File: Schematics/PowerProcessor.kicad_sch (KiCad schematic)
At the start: 0 parts

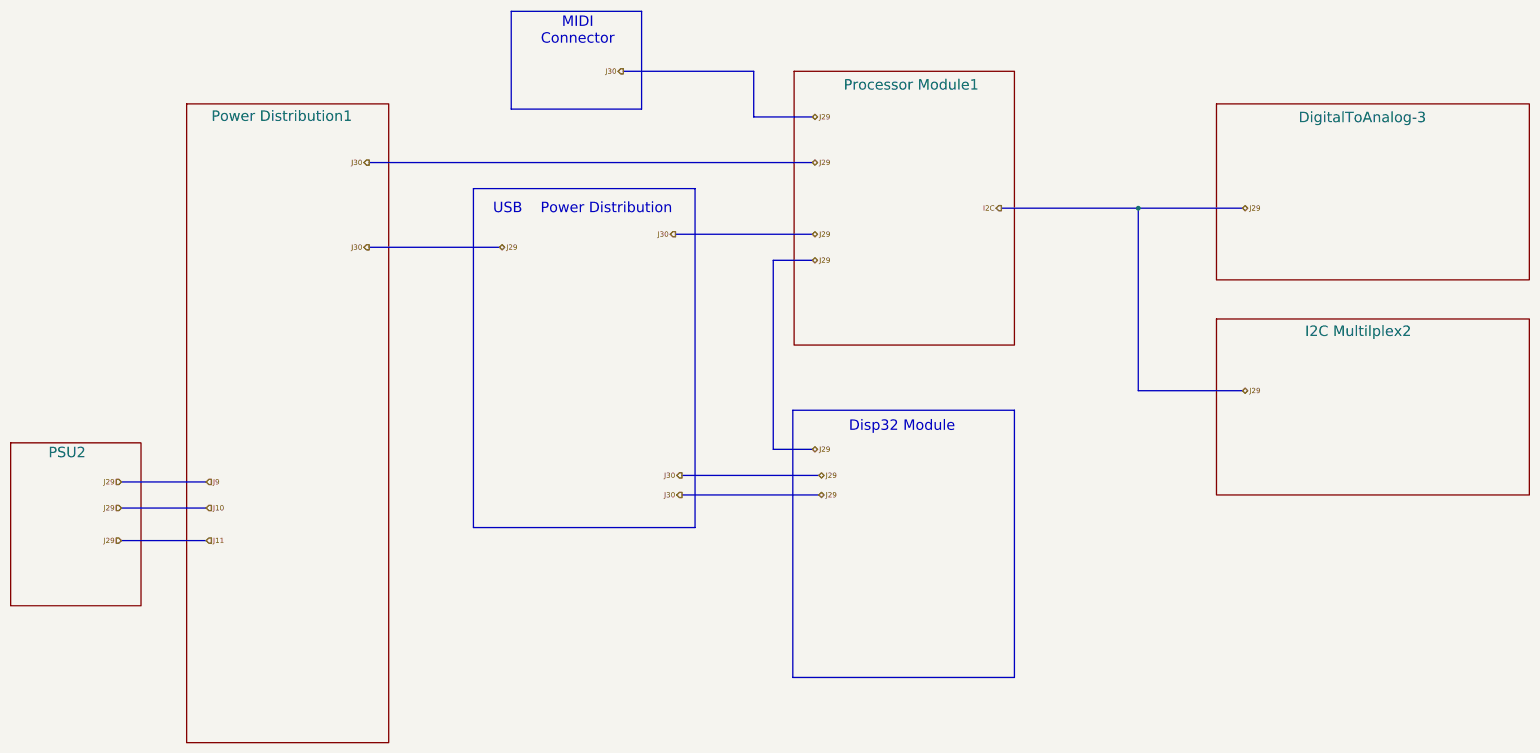
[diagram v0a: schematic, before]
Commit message: Updated schematics.  Added modulation control to VCF.
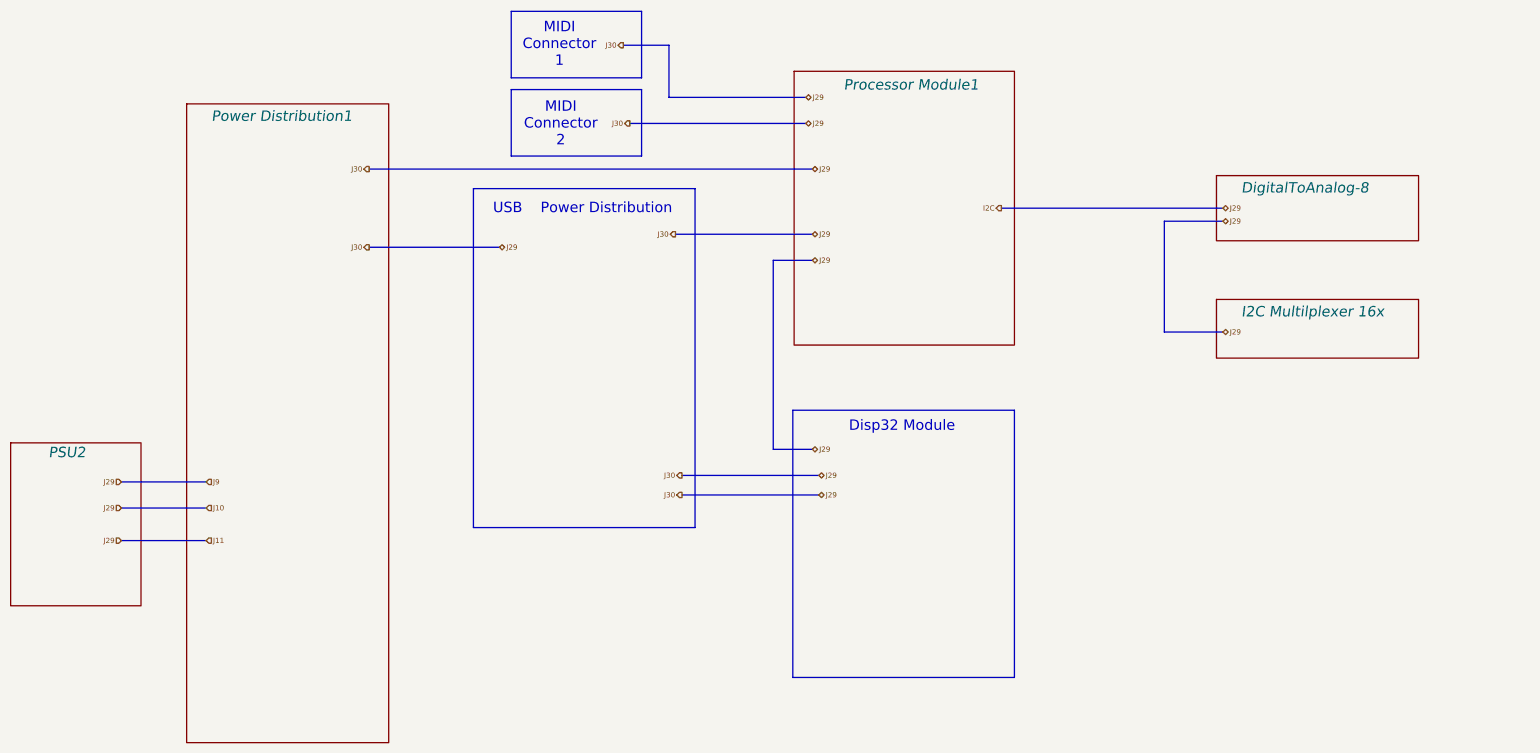
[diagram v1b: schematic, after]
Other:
- sheet DigitalToAnalog-3 renamed DigitalToAnalog-8
- sheet I2C Multilplex2 renamed I2C Multilplexer 16x
- note added: "MIDI Connector 1"
- note added: "MIDI Connector 2"
- note removed: "MIDI Connector"
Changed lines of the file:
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@@
 	(rectangle
 		(start 120.396 16.256)
-		(end 145.796 35.306)
+		(end 145.796 29.21)
 		(stroke
 			(width 0)
@@
 		)
 	)
-	(text "MIDI\nConnector"
-		(exclude_from_sim no)
-		(at 133.35 22.86 0)
+	(rectangle
+		(start 120.396 31.496)
+		(end 145.796 44.45)
+		(stroke
+			(width 0)
+			(type default)
+		)
+		(fill
+			(type none)
+		)
+	)
+	(text "MIDI\nConnector\n1"
+		(exclude_from_sim no)
+		(at 129.794 27.178 0)
 		(effects
 			(font
@@
 		)
 	)
+	(text "MIDI\nConnector\n2\n"
+		(exclude_from_sim no)
+		(at 130.048 42.672 0)
+		(effects
+			(font
+				(size 2.032 2.032)
+			)
+			(justify bottom)
+		)
+	)
 	(text "USB	Power Distribution"
 		(exclude_from_sim no)
@@
 		)
 	)
-	(junction
-		(at 242.57 54.61)
-		(diameter 0)
-		(color 0 0 0 0)
-	)
 	(bus
 		(pts
@@
 	(bus
 		(pts
-			(xy 167.64 36.83) (xy 167.64 27.94)
-		)
-		(stroke
-			(width 0)
-			(type default)
-		)
-	)
-	(bus
-		(pts
-			(xy 262.89 54.61) (xy 242.57 54.61)
-		)
-		(stroke
-			(width 0)
-			(type default)
-		)
-	)
-	(bus
-		(pts
-			(xy 167.64 27.94) (xy 142.24 27.94)
+			(xy 259.08 57.15) (xy 247.65 57.15)
+		)
+		(stroke
+			(width 0)
+			(type default)
+		)
+	)
+	(bus
+		(pts
+			(xy 151.13 33.02) (xy 151.13 22.86)
+		)
+		(stroke
+			(width 0)
+			(type default)
+		)
+	)
+	(bus
+		(pts
+			(xy 151.13 22.86) (xy 142.24 22.86)
 		)
 		(stroke
@@
 	(bus
 		(pts
-			(xy 242.57 90.17) (xy 262.89 90.17)
-		)
-		(stroke
-			(width 0)
-			(type default)
-		)
-	)
-	(bus
-		(pts
-			(xy 167.64 36.83) (xy 179.07 36.83)
+			(xy 247.65 57.15) (xy 247.65 78.74)
+		)
+		(stroke
+			(width 0)
+			(type default)
+		)
+	)
+	(bus
+		(pts
+			(xy 151.13 33.02) (xy 177.8 33.02)
 		)
 		(stroke
@@
 	(bus
 		(pts
-			(xy 242.57 54.61) (xy 242.57 90.17)
-		)
-		(stroke
-			(width 0)
-			(type default)
-		)
-	)
-	(bus
-		(pts
-			(xy 92.71 45.72) (xy 179.07 45.72)
+			(xy 92.71 46.99) (xy 179.07 46.99)
+		)
+		(stroke
+			(width 0)
+			(type default)
+		)
+	)
+	(bus
+		(pts
+			(xy 247.65 78.74) (xy 259.08 78.74)
+		)
+		(stroke
+			(width 0)
+			(type default)
+		)
+	)
+	(bus
+		(pts
+			(xy 143.51 38.1) (xy 177.8 38.1)
 		)
 		(stroke
@@
 	(bus
 		(pts
-			(xy 242.57 54.61) (xy 215.9 54.61)
+			(xy 215.9 54.61) (xy 259.08 54.61)
 		)
 		(stroke
@@
 	(hierarchical_label "J29"
 		(shape bidirectional)
-		(at 262.89 54.61 0)
-		(effects
-			(font
-				(size 1.016 1.016)
-			)
-			(justify left)
-		)
-	)
-	(hierarchical_label "J29"
-		(shape bidirectional)
-		(at 179.07 36.83 0)
+		(at 259.08 54.61 0)
+		(effects
+			(font
+				(size 1.016 1.016)
+			)
+			(justify left)
+		)
+	)
+	(hierarchical_label "J29"
+		(shape bidirectional)
+		(at 177.8 33.02 0)
+		(effects
+			(font
+				(size 1.016 1.016)
+			)
+			(justify left)
+		)
+	)
+	(hierarchical_label "J29"
+		(shape bidirectional)
+		(at 259.08 57.15 0)
 		(effects
 			(font
@@
 	(hierarchical_label "J29"
 		(shape bidirectional)
-		(at 179.07 45.72 0)
+		(at 179.07 46.99 0)
 		(effects
 			(font
@@
 	(hierarchical_label "J30"
 		(shape output)
-		(at 142.24 27.94 180)
+		(at 142.24 22.86 180)
 		(effects
 			(font
@@
 		)
 	)
-	(hierarchical_label "J29"
-		(shape bidirectional)
-		(at 262.89 90.17 0)
+	(hierarchical_label "J30"
+		(shape output)
+		(at 143.51 38.1 180)
+		(effects
+			(font
+				(size 1.016 1.016)
+			)
+			(justify right)
+		)
+	)
+	(hierarchical_label "J29"
+		(shape bidirectional)
+		(at 259.08 78.74 0)
 		(effects
 			(font
@@
 	(hierarchical_label "J29"
 		(shape bidirectional)
+		(at 177.8 38.1 0)
+		(effects
+			(font
+				(size 1.016 1.016)
+			)
+			(justify left)
+		)
+	)
+	(hierarchical_label "J29"
+		(shape bidirectional)
 		(at 118.11 62.23 0)
 		(effects
@@
 	(hierarchical_label "J30"
 		(shape output)
-		(at 92.71 45.72 180)
+		(at 92.71 46.99 180)
 		(effects
 			(font
@@
 				(font
 					(size 2.032 2.032)
+					(thickness 0.254)
+					(italic yes)
 				)
 				(justify left bottom)
@@
 	)
 	(sheet
-		(at 257.81 76.2)
-		(size 60.96 34.29)
+		(at 257.81 72.39)
+		(size 39.37 11.43)
 		(exclude_from_sim no)
 		(in_bom yes)
@@
 			(color 0 0 0 0.0000)
 		)
-		(property "Sheetname" "I2C Multilplex2"
-			(at 275.082 79.756 0)
+		(property "Sheetname" "I2C Multilplexer 16x"
+			(at 262.636 75.946 0)
 			(effects
 				(font
 					(size 2.032 2.032)
+					(thickness 0.254)
+					(italic yes)
 				)
 				(justify left bottom)
@@
 		)
 		(property "Sheetfile" "I2C_Multiplax.kicad_sch"
-			(at 257.81 125.0446 0)
+			(at 257.81 121.2346 0)
 			(effects
 				(font
@@
 	)
 	(sheet
-		(at 257.81 34.29)
-		(size 60.96 34.29)
+		(at 257.81 48.26)
+		(size 39.37 12.7)
 		(exclude_from_sim no)
 		(in_bom yes)
@@
 			(color 0 0 0 0.0000)
 		)
-		(property "Sheetname" "DigitalToAnalog-3"
-			(at 273.812 38.1 0)
+		(property "Sheetname" "DigitalToAnalog-8"
+			(at 262.636 51.816 0)
 			(effects
 				(font
 					(size 2.032 2.032)
+					(thickness 0.254)
+					(italic yes)
 				)
 				(justify left bottom)
@@
 		)
 		(property "Sheetfile" "Analog-1.kicad_sch"
-			(at 260.1214 104.648 0)
+			(at 260.1214 118.618 0)
 			(effects
 				(font
@@
 				(font
 					(size 2.032 2.032)
+					(thickness 0.254)
+					(italic yes)
 				)
 				(justify left bottom)
@@
 				(font
 					(size 2.032 2.032)
+					(thickness 0.254)
+					(italic yes)
 				)
 				(justify left bottom)
